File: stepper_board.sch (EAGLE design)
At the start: 4 parts

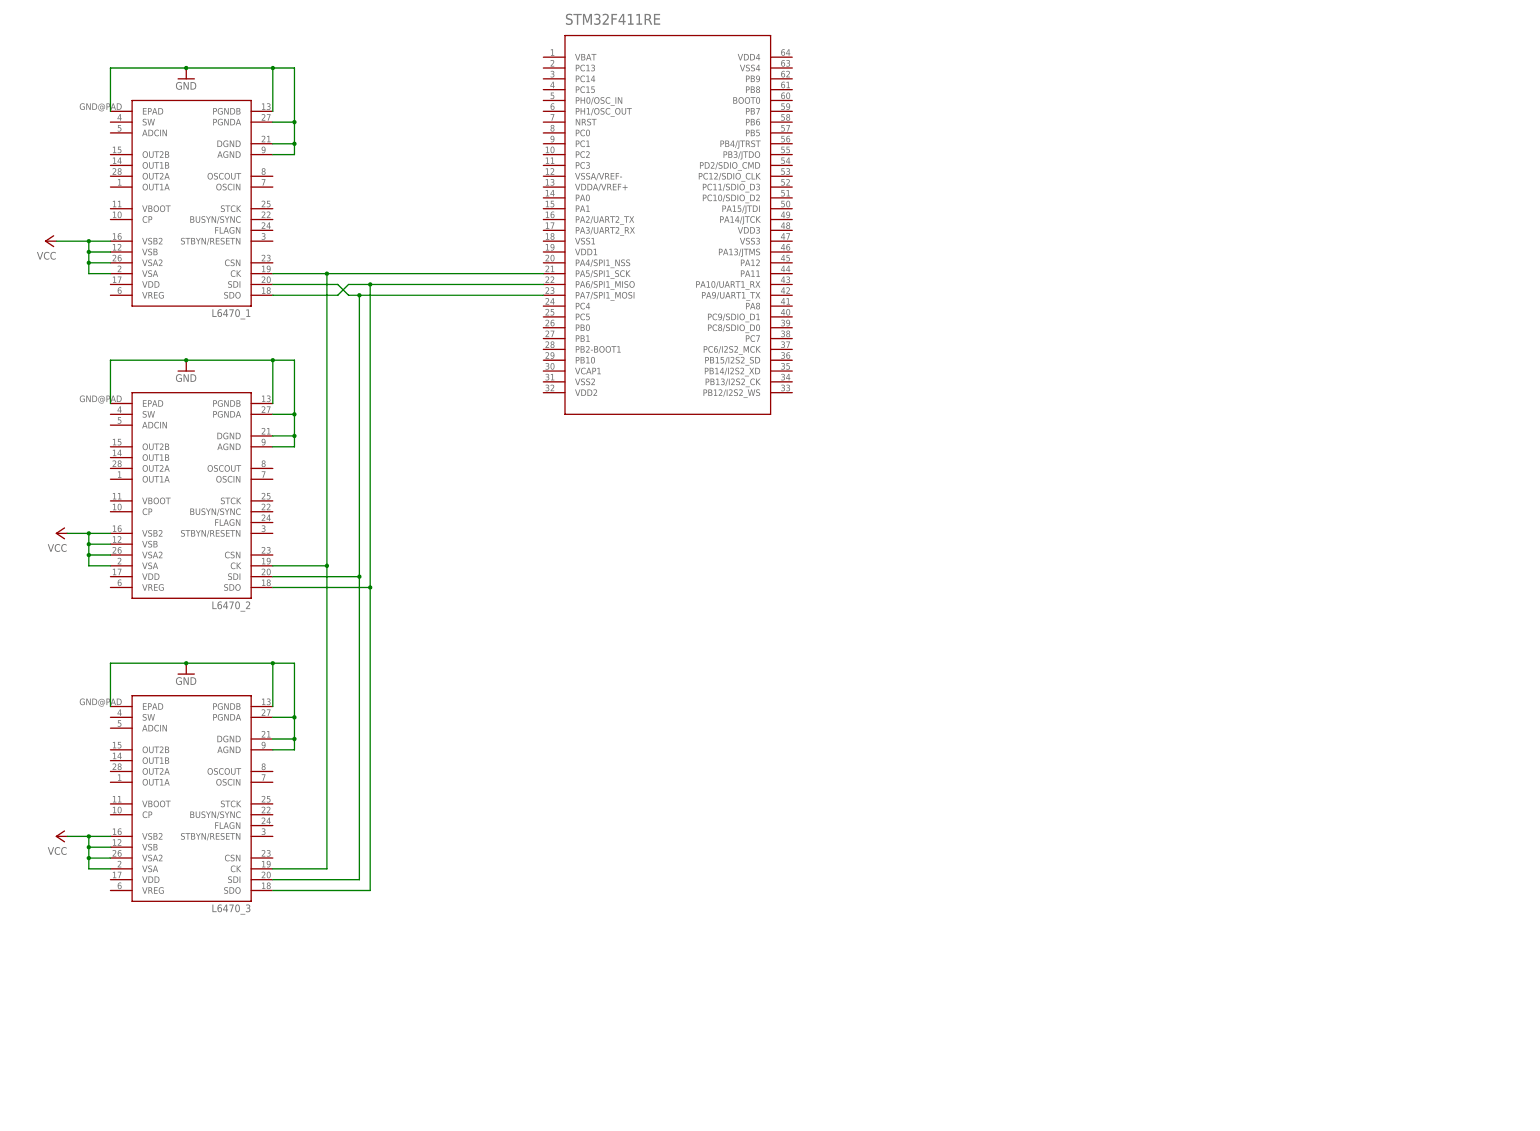
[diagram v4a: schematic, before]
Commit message: Added more connections to stepper drivers on schematic
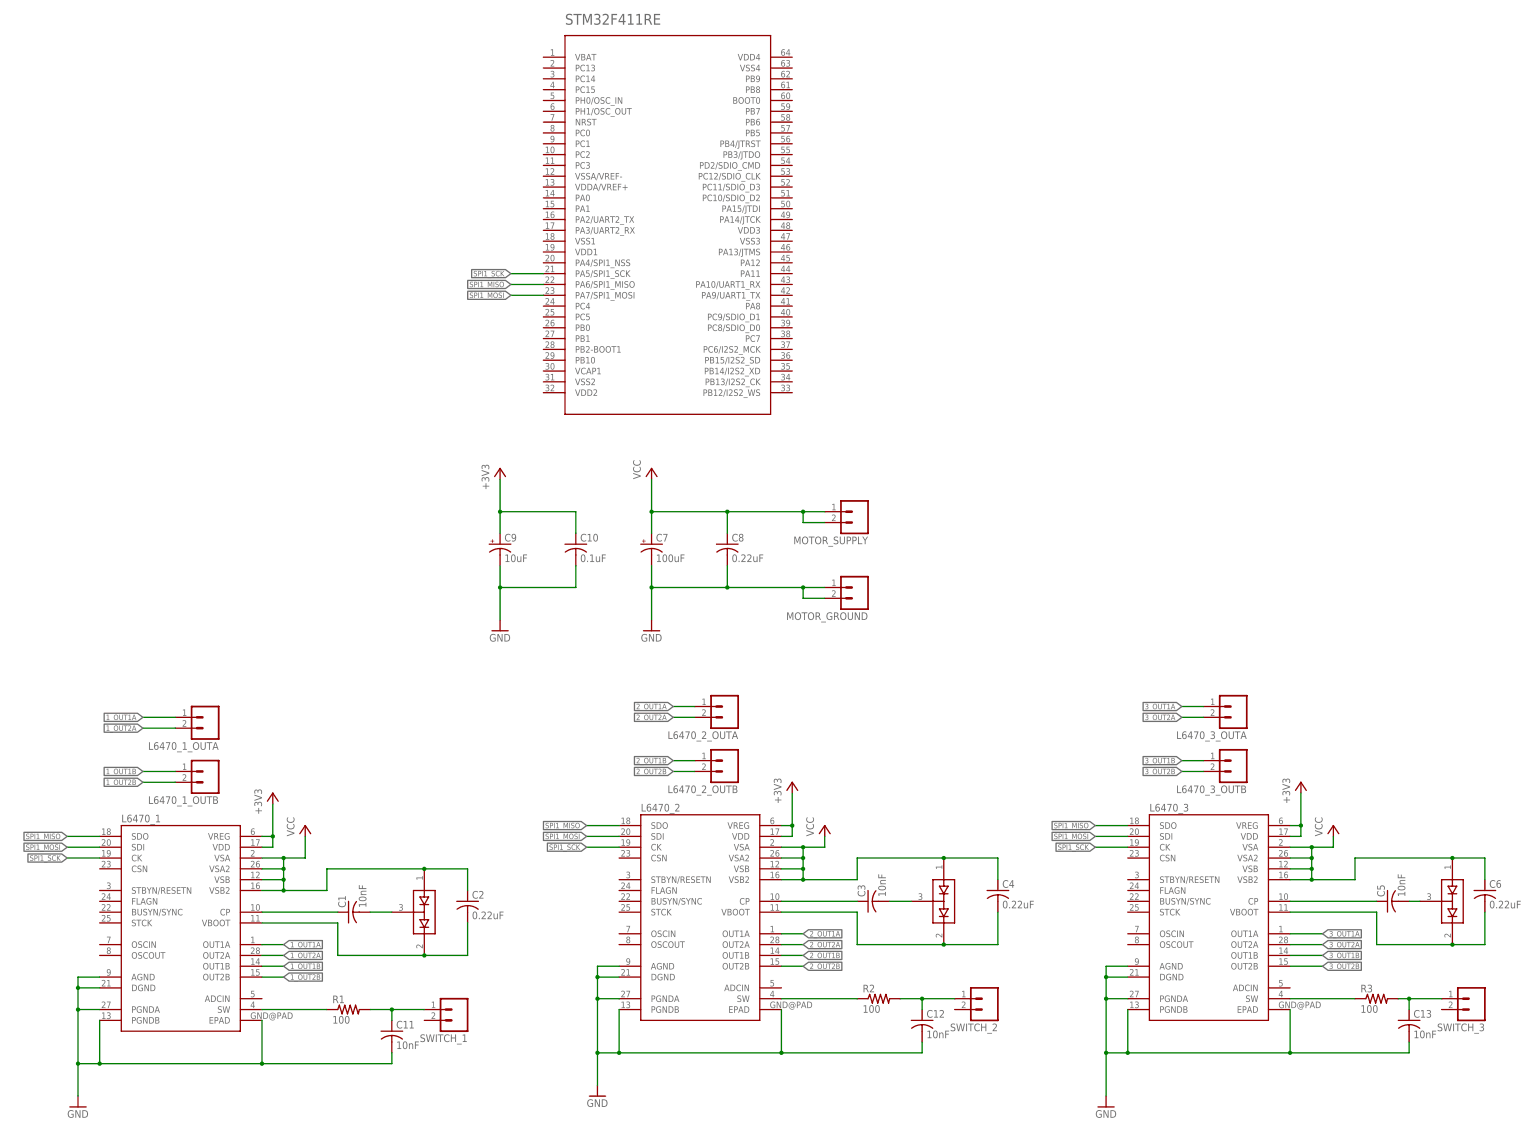
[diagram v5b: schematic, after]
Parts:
- added C1, C11, C12, C13, C3, C5: 10nF, rcl:C-USC0805
- added C10: 0.1uF, rcl:C-USC0805
- added C2, C4, C6, C8: 0.22uF, rcl:C-USC0805
- added C7: 100uF, rcl:CPOL-USUD-10X10
- added C9: 10uF, rcl:CPOL-USUD-10X10
- added D1, D2, D3: (no value), DiscreteSemi:BAV99
- added L6470_1_OUTA, L6470_1_OUTB, L6470_2_OUTA, L6470_2_OUTB, L6470_3_OUTA, L6470_3_OUTB, MOTOR_GROUND, MOTOR_SUPPLY, SWITCH_1, SWITCH_2, SWITCH_3: (no value), con-amp-quick:M02
- added R1, R2, R3: 100, resistor:R-US_R0805
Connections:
- net N$1 renamed SPI1_SCK
- net N$2 renamed SPI1_MOSI
- net N$3 renamed SPI1_MISO
- new net +3V3: C10.1, C9.+, L6470_1.VDD, L6470_1.VREG, L6470_2.VDD, L6470_2.VREG, L6470_3.VDD, L6470_3.VREG
- new net 1_OUT1A: L6470_1.OUT1A, L6470_1_OUTA.1
- new net 1_OUT1B: L6470_1.OUT1B, L6470_1_OUTB.1
- new net 1_OUT2A: L6470_1.OUT2A, L6470_1_OUTA.2
- new net 1_OUT2B: L6470_1.OUT2B, L6470_1_OUTB.2
- new net 2_OUT1A: L6470_2.OUT1A, L6470_2_OUTA.1
- new net 2_OUT1B: L6470_2.OUT1B, L6470_2_OUTB.1
- new net 2_OUT2A: L6470_2.OUT2A, L6470_2_OUTA.2
- new net 2_OUT2B: L6470_2.OUT2B, L6470_2_OUTB.2
- new net 3_OUT1A: L6470_3.OUT1A, L6470_3_OUTA.1
- new net 3_OUT1B: L6470_3.OUT1B, L6470_3_OUTB.1
- new net 3_OUT2A: L6470_3.OUT2A, L6470_3_OUTA.2
- new net 3_OUT2B: L6470_3.OUT2B, L6470_3_OUTB.2
- new net N$1: C1.1, L6470_1.CP
- new net N$10: C6.2, D3.C2, L6470_3.VBOOT
- new net N$11: C11.1, R1.2, SWITCH_1.1
- new net N$12: L6470_2.SW, R2.1
- new net N$13: C12.1, R2.2, SWITCH_2.1
- new net N$14: L6470_3.SW, R3.1
- new net N$15: C13.1, R3.2, SWITCH_3.1
- new net N$2: C1.2, D1.COM
- new net N$3: C2.2, D1.C2, L6470_1.VBOOT
- new net N$4: C3.1, L6470_2.CP
- new net N$5: C3.2, D2.COM
- new net N$6: C4.2, D2.C2, L6470_2.VBOOT
- new net N$7: L6470_1.SW, R1.1
- new net N$8: C5.1, L6470_3.CP
- new net N$9: C5.2, D3.COM
- net GND: now also C10.2, C11.2, C12.2, C13.2, C7.-, C8.2, C9.-, MOTOR_GROUND.1, MOTOR_GROUND.2
- net VCC: now also C2.1, C4.1, C6.1, C7.+, C8.1, D1.A1, D2.A1, D3.A1, MOTOR_SUPPLY.1, MOTOR_SUPPLY.2
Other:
- moved on the sheet: L6470_1, L6470_2, L6470_3

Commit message: Added all the stuffs
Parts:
- added C14, C15: 10pF, rcl:C-USC0805
- added C16: 2.2uF, rcl:C-USC0805
- added C17, C22: 4.7uF, rcl:C-USC0805
- added C18, C20: 10uF, rcl:CPOL-USUD-10X10
- added C19, C21: 0.1uF, rcl:C-USC0805
- added C23, C24, C25, C26: 100n, rcl:C-USC0805
- added IC1: MCP1703DB, linear:MCP1703DB
- added Y1: 12 MHz, abracon:CRYSTAL.3.2X2.5MM
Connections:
- new net N$16: C14.1, STM32F411RE.PH0/OSC_IN, Y1.1
- new net N$17: C15.1, STM32F411RE.PH1/OSC_OUT, Y1.2
- new net N$18: STM32F411RE.VSS1
- new net N$19: STM32F411RE.VDD1
- new net N$20: STM32F411RE.VSS2
- new net N$21: STM32F411RE.VDD2
- new net N$22: STM32F411RE.VDD4
- new net N$23: STM32F411RE.VSS4
- new net N$24: STM32F411RE.VDD3
- new net N$25: STM32F411RE.VSS3
- new net V+: C16.1, IC1.VI
- net +3V3: now also C17.1, C18.+, C19.1, C20.+, C21.1, C22.1, C23.1, C24.1, C25.1, C26.1, IC1.VO
- net GND: now also C14.2, C15.2, C16.2, C17.2, C18.-, C19.2, C20.-, C21.2, C22.2, C23.2, C24.2, C25.2, C26.2, IC1.GND
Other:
- note added: "MCU/L6470 Power"
- note added: "Motor Power"
- moved on the sheet: C10, C7, C8, C9, MOTOR_GROUND, MOTOR_SUPPLY

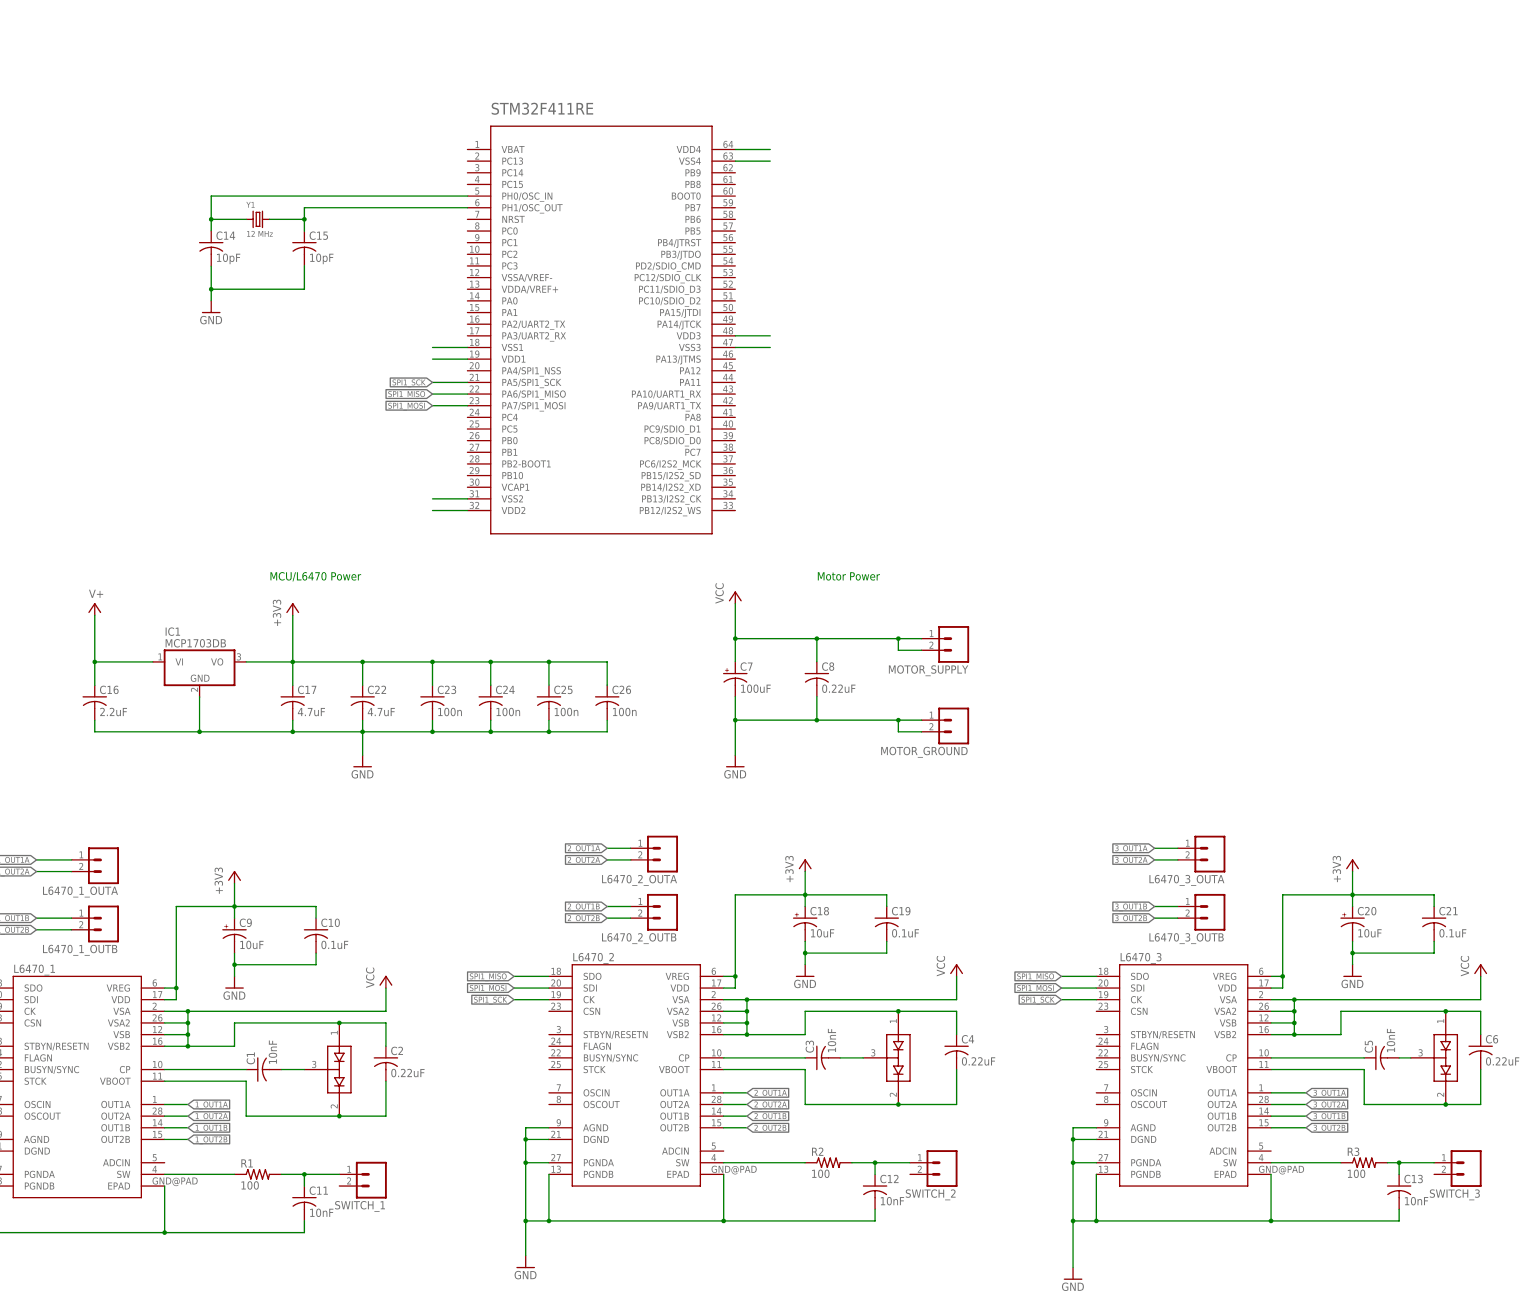
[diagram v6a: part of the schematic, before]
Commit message: Added datasheet and libraries for components. Added MicroSD, MicroUSB, and power regulation to microcontroller schematic.
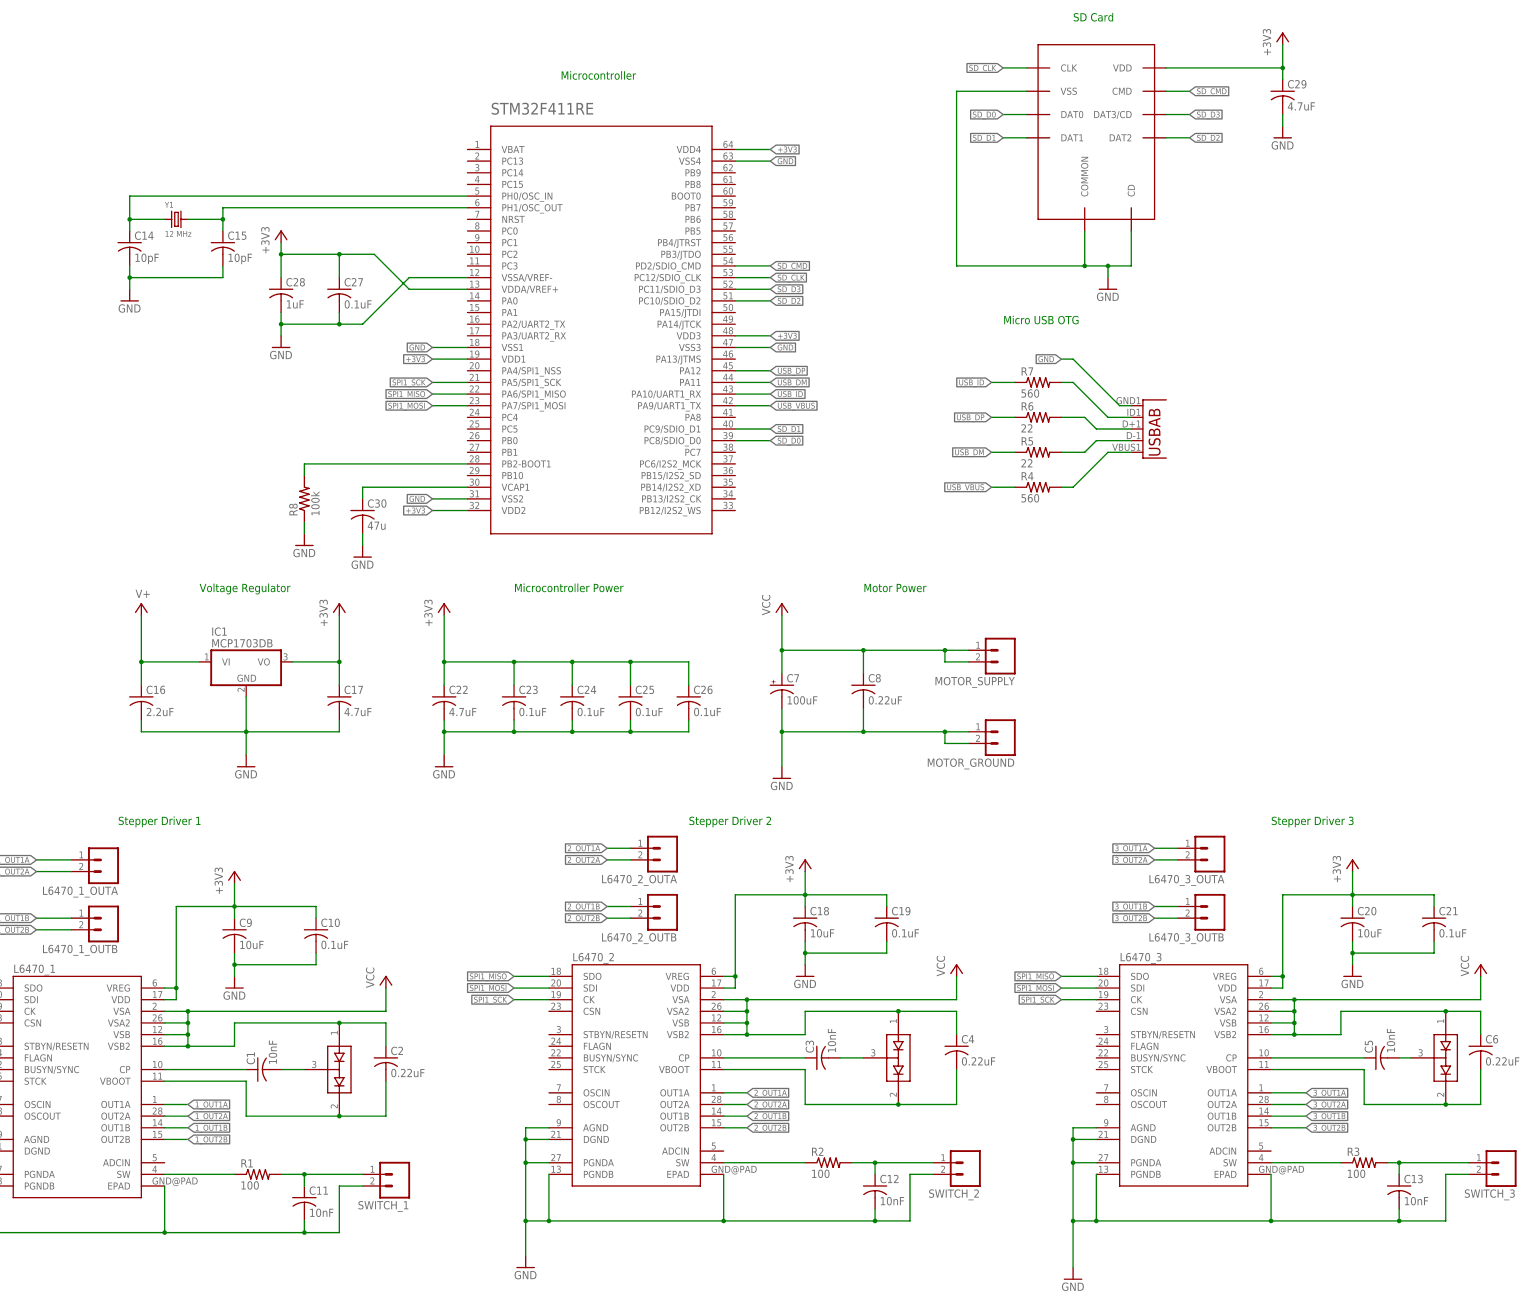
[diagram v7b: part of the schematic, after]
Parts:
- added C27: 0.1uF, rcl:C-USC0805
- added C28: 1uF, rcl:C-USC0805
- added C29: 4.7uF, rcl:C-USC0805
- added C30: 47u, rcl:C-USC0805
- added R4, R7: 560, rcl:R-US_R0805
- added R5, R6: 22, rcl:R-US_R0805
- added R8: 100k, rcl:R-US_R0805
- added SD1: SCHA5B0200, SCHA5B0200_hand:SCHA5B0200
- added U1: (no value), MicroUSB:USB""
- C18, C20, C9: device rcl:CPOL-USUD-10X10 -> rcl:C-USC0805
- C23, C24, C25, C26: value 100n -> 0.1uF
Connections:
- removed net N$24: STM32F411RE.VDD3
- removed net N$25: STM32F411RE.VSS3
- new net SD_CLK: SD1.CLK, STM32F411RE.PC12/SDIO_CLK
- new net SD_CMD: SD1.CMD, STM32F411RE.PD2/SDIO_CMD
- new net SD_D0: SD1.DAT0, STM32F411RE.PC8/SDIO_D0
- new net SD_D1: SD1.DAT1, STM32F411RE.PC9/SDIO_D1
- new net SD_D2: SD1.DAT2, STM32F411RE.PC10/SDIO_D2
- new net SD_D3: SD1.DAT3/CD, STM32F411RE.PC11/SDIO_D3
- new net USB_DM: R5.1, STM32F411RE.PA11
- new net USB_DP: R6.1, STM32F411RE.PA12
- new net USB_ID: R7.1, STM32F411RE.PA10/UART1_RX
- new net USB_VBUS: R4.1, STM32F411RE.PA9/UART1_TX
- net +3V3: now also C18.1, C20.1, C27.1, C28.1, C29.1, C9.1, SD1.VDD, STM32F411RE.VDD1, STM32F411RE.VDD2, STM32F411RE.VDD3, STM32F411RE.VDD4, STM32F411RE.VDDA/VREF+; no longer C18.+, C20.+, C9.+
- net GND: now also C18.2, C20.2, C27.2, C28.2, C29.2, C30.2, C9.2, R8.1, SD1.CD, SD1.COMMON, SD1.VSS, STM32F411RE.VSS1, STM32F411RE.VSS2, STM32F411RE.VSS3, STM32F411RE.VSS4, STM32F411RE.VSSA/VREF-, SWITCH_1.2, SWITCH_2.2, SWITCH_3.2, U1.GND; no longer C18.-, C20.-, C9.-
- net N$18: now also R4.2, U1.VBUS; no longer STM32F411RE.VSS1
- net N$19: now also R5.2, U1.D-; no longer STM32F411RE.VDD1
- net N$20: now also R6.2, U1.D+; no longer STM32F411RE.VSS2
- net N$21: now also R7.2, U1.USBID; no longer STM32F411RE.VDD2
- net N$22: now also C30.1, STM32F411RE.VCAP1; no longer STM32F411RE.VDD4
- net N$23: now also R8.2, STM32F411RE.PB2-BOOT1; no longer STM32F411RE.VSS4
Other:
- note added: "Micro USB OTG"
- note added: "Microcontroller"
- note added: "Microcontroller Power"
- note added: "SD Card"
- note added: "Stepper Driver 1"
- note added: "Stepper Driver 2"
- note added: "Stepper Driver 3"
- note added: "Voltage Regulator"
- note removed: "MCU/L6470 Power"
- moved on the sheet: C14, C15, C16, C17, C22, C23, C24, C25, C26, C7, C8, IC1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
